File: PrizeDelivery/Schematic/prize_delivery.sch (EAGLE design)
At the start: 13 parts, among them Q1 IRL540

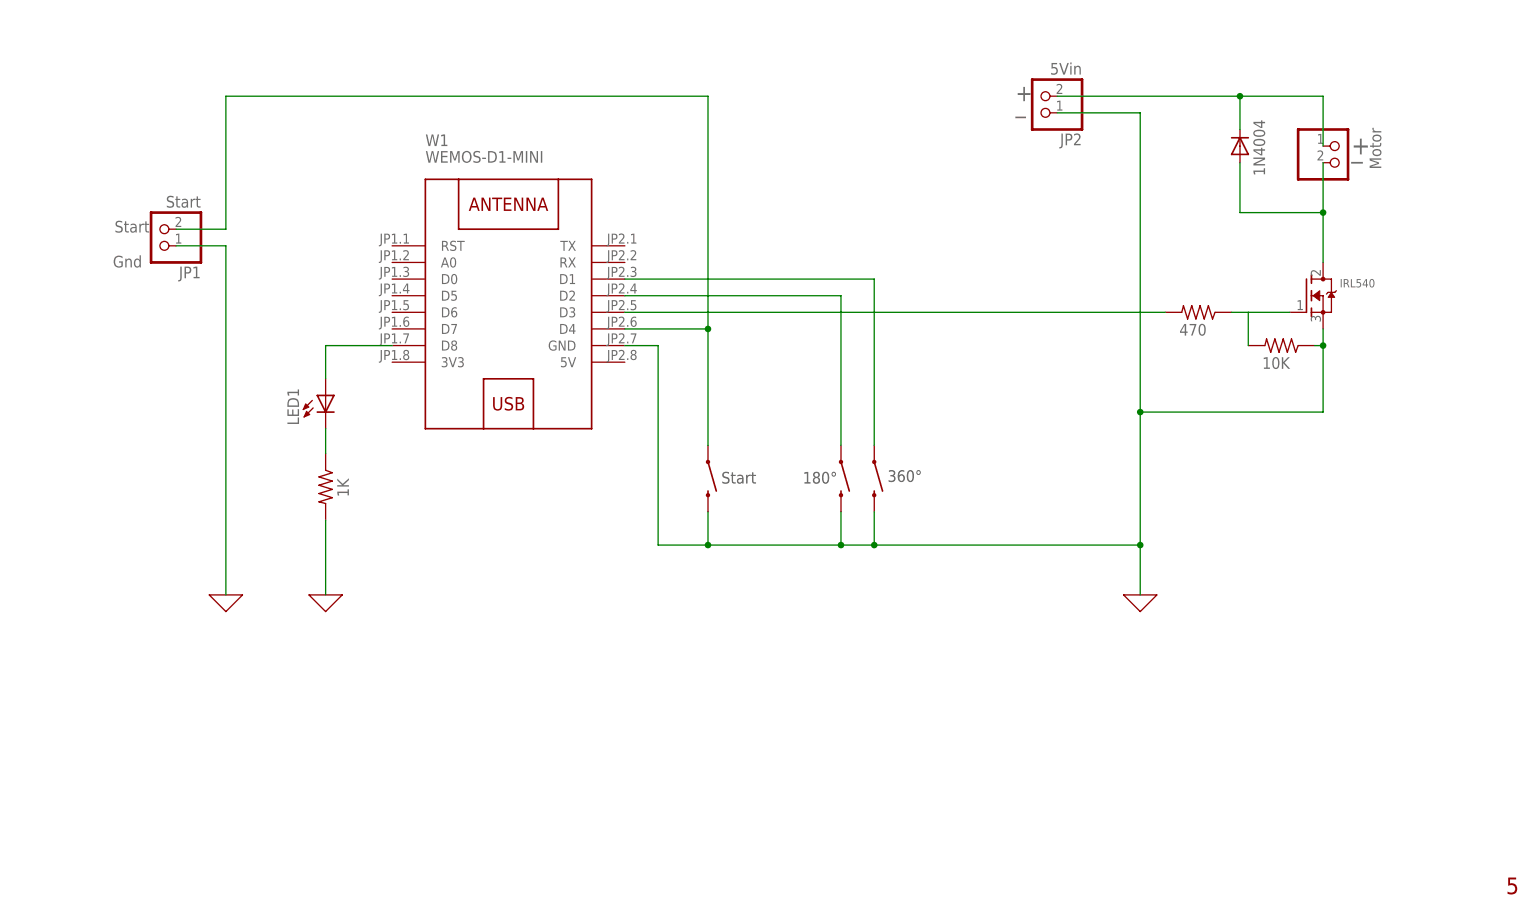
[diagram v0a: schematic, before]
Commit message: Added images folder
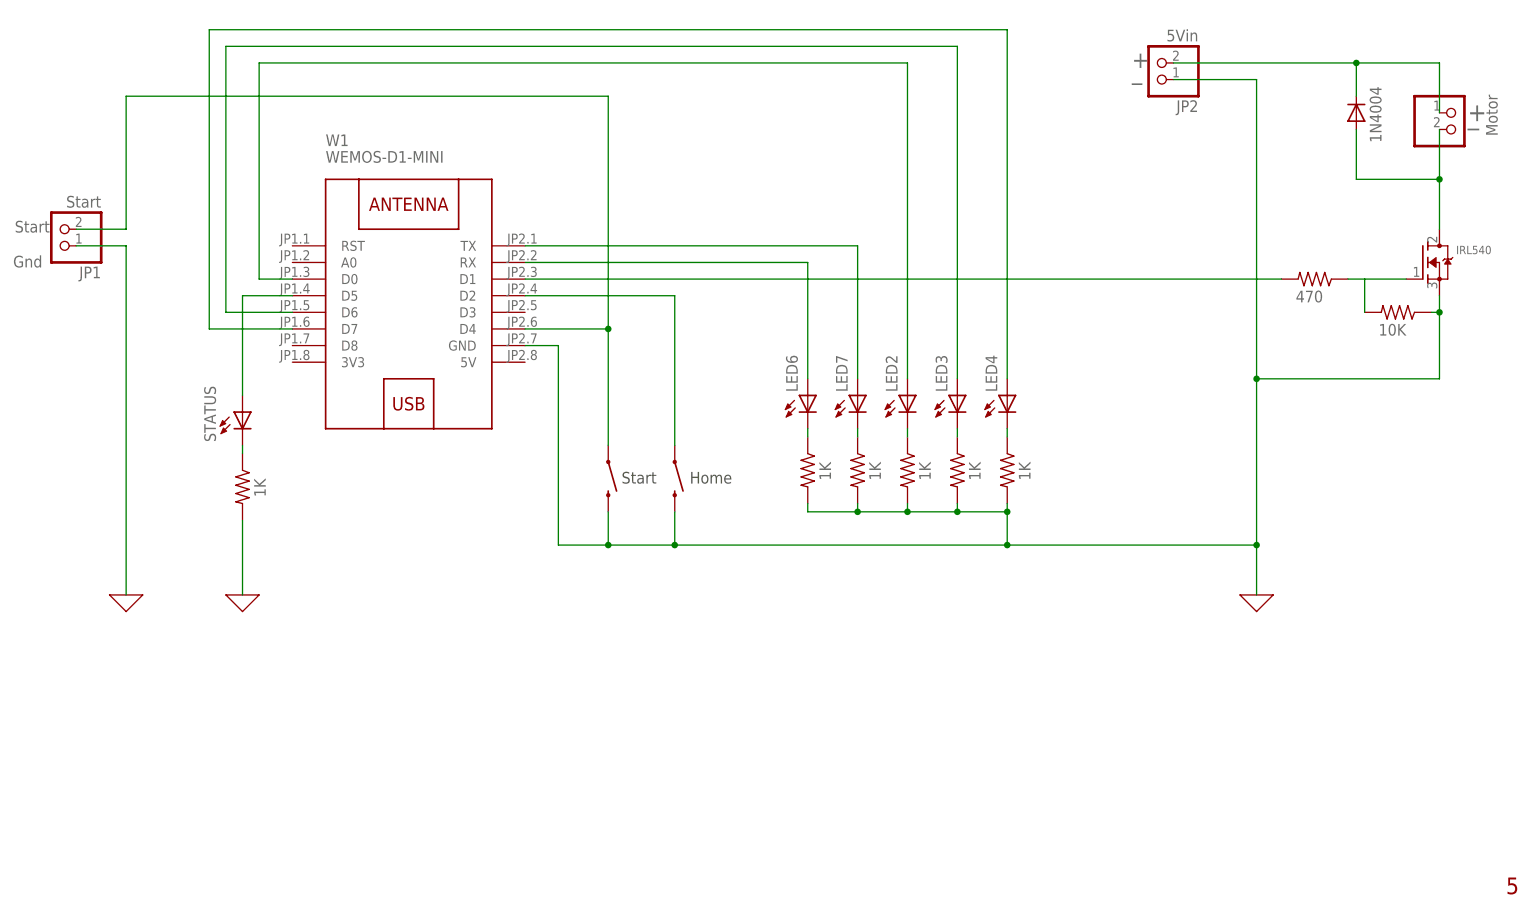
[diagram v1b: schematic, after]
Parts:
- removed 180°: MOMENTARY-SWITCH-SPST-PTH-6.0MM, SparkFun-Switches:MOMENTARY-SWITCH-SPST-PTH-6.0MM
- removed LED1: (no value), adafruit:LED5MM
- added LED2, LED3, LED4, LED6, LED7, STATUS: (no value), adafruit:LED5MM
- added R3, R5, R6, R8, R9: 1K, adafruit:R-US_0207/10
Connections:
- new net N$11: LED6.C, R8.1
- new net N$12: LED7.C, R9.1
- new net N$15: LED2.A, W1.D0
- new net N$16: LED3.A, W1.D6
- new net N$17: LED4.A, W1.D7
- new net N$18: LED7.A, W1.TX
- new net N$19: LED6.A, W1.RX
- new net N$20: STATUS.A, W1.D5
- new net N$8: LED4.C, R6.1
- net 0: now also R3.2, R5.2, R6.2, R8.2, R9.2; no longer 180°.2
- net N$1: now also LED2.C, R3.1; no longer R2.2, W1.D3
- net N$4: now also LED3.C, R5.1; no longer 180°.1, W1.D2
- net N$5: now also W1.D2; no longer W1.D1
- net N$6: now also R2.2, W1.D1; no longer LED1.A, W1.D8
- net N$7: now also STATUS.C; no longer LED1.C
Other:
- note added: "Home"
- note removed: "180°"
- note removed: "360°"
- moved on the sheet: JP1, JP2, W1

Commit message: Not sure
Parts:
- removed LED2, LED3, LED4, LED6, LED7, STATUS: (no value), adafruit:LED5MM
- removed R1, R3, R5, R6, R8, R9: 1K, adafruit:R-US_0207/10
- added J2: (no value), Wurth_Elektronik_Electromechanic_Terminal_Blocks_Connectors_rev19b:691136710008
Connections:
- removed net N$1: LED2.C, R3.1
- removed net N$11: LED6.C, R8.1
- removed net N$12: LED7.C, R9.1
- removed net N$4: LED3.C, R5.1
- removed net N$7: R1.1, STATUS.C
- removed net N$8: LED4.C, R6.1
- net 0: now also J2.1; no longer R1.2, R3.2, R5.2, R6.2, R8.2, R9.2
- net N$15: now also J2.4; no longer LED2.A
- net N$16: now also J2.5; no longer LED3.A
- net N$17: now also J2.6; no longer LED4.A
- net N$18: now also J2.8; no longer LED7.A
- net N$19: now also J2.7; no longer LED6.A
- net N$20: now also J2.3; no longer STATUS.A
- net N$9: now also J2.2
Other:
- note added: "LED1, "Locate""
- note added: "LED2, "Verify""
- note added: "LED3, "Retreive""
- note added: "LED4, "Transport""
- note added: "LED5, "Delivery""
- note added: "Status"
- moved on the sheet: JP2
